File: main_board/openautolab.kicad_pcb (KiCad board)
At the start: 2 copper layers, 148.6 x 118.1 mm, 32 parts, among them J1 PIN11, J10 HX711, J11 LCD, J12 OUT+, J13 OUT-, J14 IN+, J15 IN-, J16 PWR_IN, J17 FILTER_PUMP, J18 FILTER_SENSOR, J2 PIN9, J3 PIN10, J4 PIN12, J6 PIN7, J7 PIN8, J8 PUMP, J9 SERVO, K1 FINDER-36.11, K2 FINDER-36.11, SW0 PIN_A0, SW1 PIN_A1, SW2 PIN_A2, SW3 SW_SPDT, U1 TD62064APG, U2 TD62064APG

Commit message: frame upgrades
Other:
- board size 148.6 x 118.1 mm -> 157.5 x 124.5 mm
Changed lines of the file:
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@@
     )
     (pad_to_mask_clearance 0)
+    (aux_axis_origin 27.94 22.86)
+    (grid_origin 27.94 22.86)
     (pcbplotparams
       (layerselection 0x00010fc_ffffffff)
@@
     )
   )
-  (gr_rect (start 32.38 27.3) (end 180.97 145.41) (layer "Edge.Cuts") (width 0.1) (fill none))
+  (gr_rect (start 39.37 93.98) (end 114.3 125.73) (layer "Dwgs.User") (width 0.15) (fill none))
+  (gr_rect (start 27.94 22.86) (end 185.42 147.32) (layer "Edge.Cuts") (width 0.1) (fill none))
   (segment (start 117.475 95.875) (end 120.01 95.875) (width 0.5) (layer "B.Cu") (net 4))
   (segment (start 36.195 142.87) (end 36.2 142.865) (width 0.5) (layer "B.Cu") (net 4))
@@
     (connect_pads (clearance 2))
     (min_thickness 1) (filled_areas_thickness no)
-    (fill yes (thermal_gap 0.508) (thermal_bridge_width 1) (island_removal_mode 2) (island_area_min 25))
+    (fill (thermal_gap 0.508) (thermal_bridge_width 1) (island_removal_mode 2) (island_area_min 25))
     (polygon
       (pts
-        (xy 180.97 145.41)
-        (xy 32.38 145.41)
-        (xy 32.38 27.3)
-        (xy 180.97 27.3)
+        (xy 185.42 147.32)
+        (xy 27.94 147.32)
+        (xy 27.94 22.86)
+        (xy 185.42 22.86)
       )
     )

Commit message: update PCB
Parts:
- removed J12: OUT+, Connector_PinHeader_2.54mm:PinHeader_1x01_P2.54mm_Vertical
- removed J13: OUT-, Connector_PinHeader_2.54mm:PinHeader_1x01_P2.54mm_Vertical
- removed J14: IN+, Connector_PinHeader_2.54mm:PinHeader_1x01_P2.54mm_Vertical
- removed J15: IN-, Connector_PinHeader_2.54mm:PinHeader_1x01_P2.54mm_Vertical
- added C1: C_Polarized, Capacitor_THT:CP_Radial_D10.0mm_P5.00mm, F.Cu at (147.3, 86.4)
- added C2: C_Polarized, Capacitor_THT:CP_Radial_D8.0mm_P5.00mm, F.Cu at (154.9, 59.8)
- added D6: 1N5822, Diode_THT:D_DO-201AD_P15.24mm_Horizontal, F.Cu at (145.4, 71.1)
- added L1: L, Inductor_THT:L_Toroid_Vertical_L26.7mm_W14.0mm_P10.16mm_Pulse_D, F.Cu at (172.7, 66.6)
- added NT1: NetTie_2, NetTie:NetTie-2_SMD_Pad2.0mm, F.Cu at (160.7, 50.8)
- added U3: LM2576T-5, Package_TO_SOT_THT:TO-220-5_Vertical, F.Cu at (151.7, 68.9)
- J16: value PWR_IN -> - PWR_IN +
- SW3: value SW_SPDT -> SW_DPST_x2; footprint Button_Switch_THT:SW_Slide_1P2T_CK_OS102011MS2Q -> Connector_PinHeader_2.54mm:PinHeader_1x02_P2.54mm_Vertical
- moved SW3 133.7 mm to (40.6, 58.4), turned to 180 degrees
- moved J17 89.8 mm to (148.6, 44.8), turned to 0 degrees
- moved D5 89.5 mm to (142.5, 54.5), turned to -90 degrees
- moved J18 80.1 mm to (135.9, 44.8), turned to 0 degrees
- moved A1 74.5 mm to (135.9, 111.8), turned to 90 degrees
- moved K2 62.4 mm to (104.1, 71.1)
- moved J9 60.4 mm to (40.6, 71.1), turned to 180 degrees
- moved K1 60.1 mm to (83.8, 71.1)
- moved J2 49.2 mm to (47.0, 44.8)
- moved J10 48.5 mm to (72.2, 92.7)
- moved J11 46.6 mm to (91.4, 92.7)
- moved BZ0 45.3 mm to (133.4, 83.8), turned to 0 degrees
- moved U1 42.8 mm to (69.7, 72.3), turned to 180 degrees
- moved SW2 33.8 mm to (131.8, 116.9)
- moved SW0 33.8 mm to (70.9, 117.2)
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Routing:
- net +12V: track 595.9 -> 250.1 mm, vias 0 -> 1
- net GNDPWR: track 382.9 -> 184.2 mm, vias 4 -> 1
- net Net-(A1-Pad5): track 224.5 -> 89.8 mm
- net Net-(A1-Pad6): track 225.7 -> 91.2 mm
- net Net-(D5-Pad2): track 18.5 -> 139.2 mm, vias 0 -> 1
- net Net-(A1-Pad14): track 17.5 -> 133.4 mm, vias 0 -> 2
- net GND: track 417.6 -> 305.7 mm, vias 4 -> 1
- net Net-(A1-Pad15): track 42.9 -> 145.2 mm, vias 2 -> 1
- net Net-(A1-Pad13): track 56.3 -> 150.9 mm, vias 2 -> 0
- net Net-(A1-Pad7): track 46.5 -> 135.7 mm
- net Net-(J18-Pad2): track 19.9 -> 107.6 mm
- net Net-(A1-Pad12): track 46.8 -> 133.7 mm, vias 0 -> 1
- net Net-(A1-Pad21): track 123.3 -> 37.3 mm
- net +5V: track 226.7 -> 157.1 mm, vias 0 -> 2
- net Net-(J4-Pad1): track 13.9 -> 61.9 mm
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- removed copper zone on B.Cu, net GNDPWR
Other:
- board size 157.5 x 124.5 mm -> 144.8 x 88.9 mm

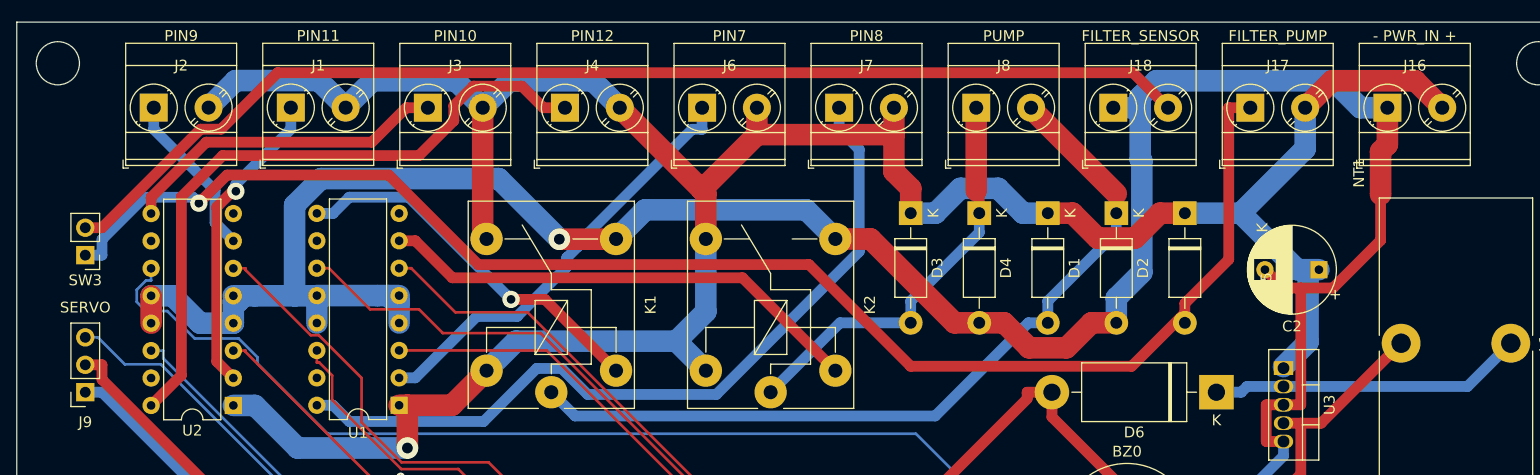
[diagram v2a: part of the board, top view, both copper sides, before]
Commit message: update schematic add power switch
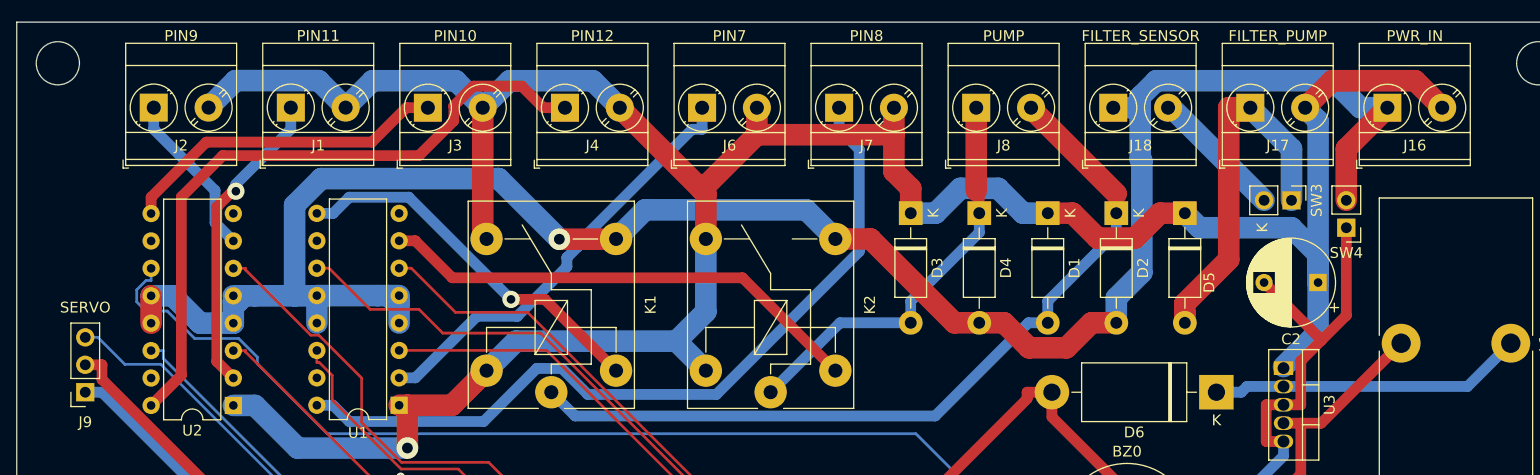
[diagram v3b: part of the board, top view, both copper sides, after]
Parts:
- removed NT1: NetTie_2, NetTie:NetTie-2_SMD_Pad2.0mm
- added SW4: SW_DPST_x2, Connector_PinHeader_2.54mm:PinHeader_1x02_P2.54mm_Vertical, F.Cu at (157.5, 55.9)
- J16: value - PWR_IN + -> PWR_IN
- moved SW3 111.9 mm to (152.4, 53.3), turned to -90 degrees
- moved C2 1.20 mm to (154.9, 61.0)
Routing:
- net Net-(D5-A): track 139.2 -> 33.8 mm, vias 1 -> 0
- net Net-(J18-Pin_2): track 107.6 -> 12.4 mm
- net GNDPWR: track 184.2 -> 190.0 mm
- net +12V: track 250.1 -> 255.7 mm
- net GND: track 305.7 -> 303.0 mm

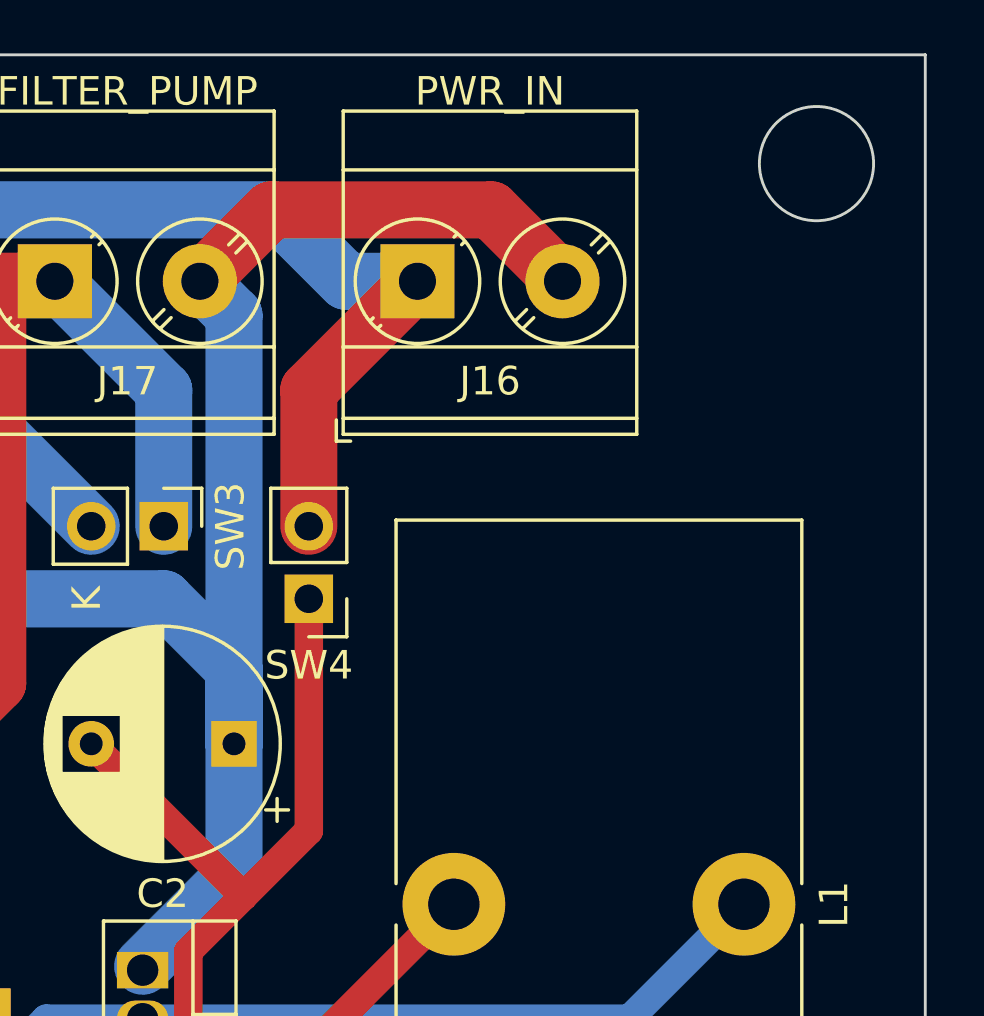
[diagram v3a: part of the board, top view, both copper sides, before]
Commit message: fixed power switch on board
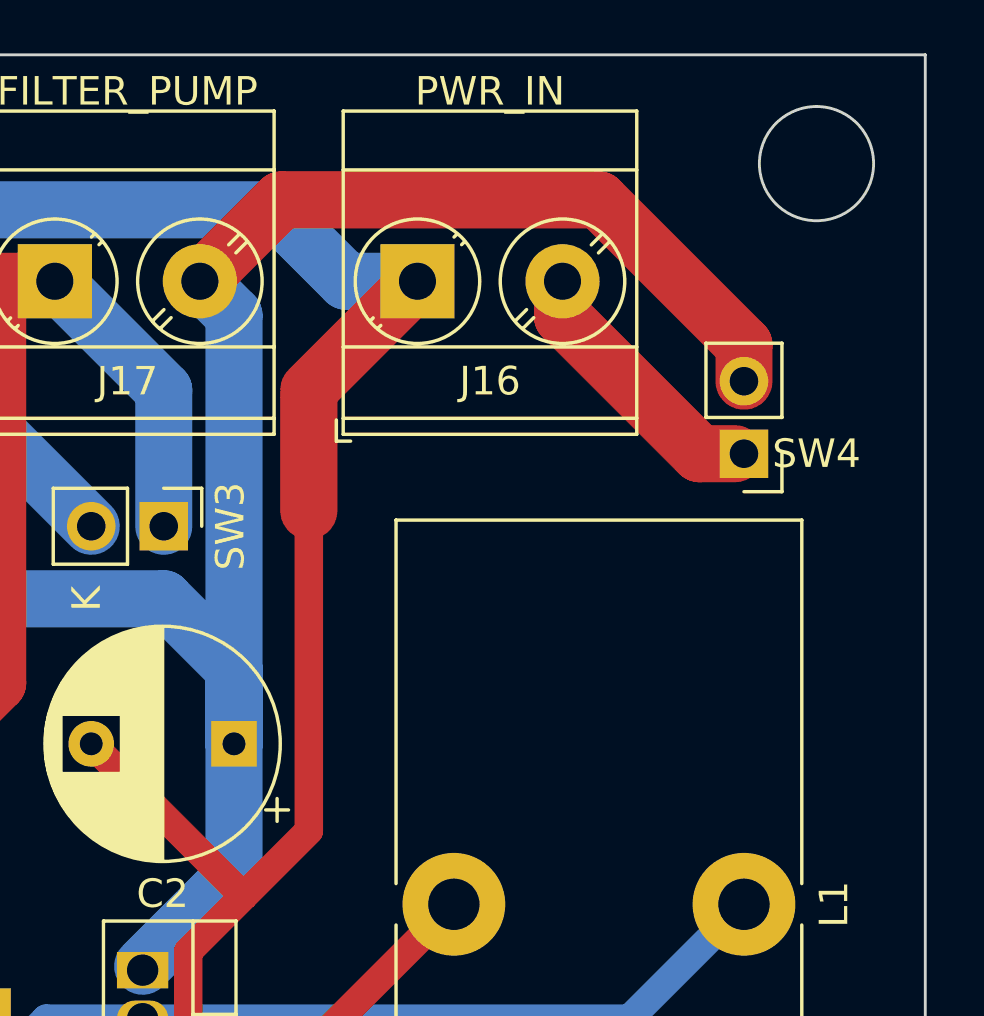
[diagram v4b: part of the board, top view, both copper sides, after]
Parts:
- added NT1: NetTie_2, NetTie:NetTie-2_SMD_Pad2.0mm, F.Cu at (157.5, 50.8)
- moved SW4 16.1 mm to (172.7, 50.8)
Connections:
- J16 pad 2: +12V -> Net-(J16-Pin_2)
- SW4 pad 1: GND -> Net-(J16-Pin_2)
- SW4 pad 2: GNDPWR -> +12V
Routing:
- net Net-(J16-Pin_2): track 0.00 -> 9.58 mm
- net +12V: track 255.7 -> 264.5 mm
- net GNDPWR: track 190.0 -> 185.2 mm
- net GND: track 303.0 -> 306.1 mm
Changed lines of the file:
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@@
   (net 43 "Net-(U1-O2)")
   (net 44 "GNDPWR")
+  (net 45 "Net-(J16-Pin_2)")
   (footprint "TerminalBlock_Phoenix:TerminalBlock_Phoenix_MKDS-3-2-5.08_1x02_P5.08mm_Horizontal" (layer "F.Cu")
     (at 161.285 44.76)
@@
       (net 44 "GNDPWR") (pinfunction "Pin_1") (pintype "passive"))
     (pad "2" thru_hole circle (at 5.08 0) (size 2.6 2.6) (drill 1.3) (layers "F&B.Cu" "*.Mask")
-      (net 42 "+12V") (pinfunction "Pin_2") (pintype "passive"))
+      (net 45 "Net-(J16-Pin_2)") (pinfunction "Pin_2") (pintype "passive"))
     (model "${KICAD6_3DMODEL_DIR}/TerminalBlock_Phoenix.3dshapes/TerminalBlock_Phoenix_MKDS-3-2-5.08_1x02_P5.08mm_Horizontal.wrl"
       (offset (xyz 0 0 0))
@@
   )
   (footprint "Connector_PinHeader_2.54mm:PinHeader_1x02_P2.54mm_Vertical" (layer "F.Cu")
-    (at 157.48 55.88 180)
+    (at 172.72 50.8 180)
     (descr "Through hole straight pin header, 1x02, 2.54mm pitch, single row")
     (tags "Through hole pin header THT 1x02 2.54mm single row")
@@
     (property "ki_keywords" "switch lever")
     (attr through_hole)
-    (fp_text reference "SW4" (at 0 -2.33) (layer "F.SilkS")
+    (fp_text reference "SW4" (at -2.54 0) (layer "F.SilkS")
         (effects (font (size 1 1) (thickness 0.15)))
     )
@@
       (stroke (width 0.1) (type solid)) (layer "F.Fab"))
     (pad "1" thru_hole rect (at 0 0 180) (size 1.7 1.7) (drill 1) (layers "*.Cu" "*.Mask")
-      (net 30 "GND") (pinfunction "A") (pintype "passive"))
+      (net 45 "Net-(J16-Pin_2)") (pinfunction "A") (pintype "passive"))
     (pad "2" thru_hole oval (at 0 2.54 180) (size 1.7 1.7) (drill 1) (layers "*.Cu" "*.Mask")
-      (net 44 "GNDPWR") (pinfunction "B") (pintype "passive"))
+      (net 42 "+12V") (pinfunction "B") (pintype "passive"))
     (model "${KICAD6_3DMODEL_DIR}/Connector_PinHeader_2.54mm.3dshapes/PinHeader_1x02_P2.54mm_Vertical.wrl"
       (offset (xyz 0 0 0))
@@
     )
   )
+  (footprint "NetTie:NetTie-2_SMD_Pad2.0mm" (layer "F.Cu")
+    (at 157.48 50.8 90)
+    (descr "Net tie, 2 pin, 2.0mm square SMD pads")
+    (tags "net tie")
+    (property "Sheetfile" "openautolab.kicad_sch")
+    (property "Sheetname" "")
+    (property "exclude_from_bom" "")
+    (property "ki_description" "Net tie, 2 pins")
+    (property "ki_keywords" "net tie short")
+    (attr exclude_from_pos_files exclude_from_bom allow_missing_courtyard)
+    (net_tie_pad_groups "1, 2")
+    (fp_text reference "NT1" (at 0 -2 90) (layer "F.SilkS") hide
+        (effects (font (size 1 1) (thickness 0.15)))
+    )
+    (fp_text value "NetTie_2" (at 0 2 90) (layer "F.Fab") hide
+        (effects (font (size 1 1) (thickness 0.15)))
+    )
+    (fp_poly
+      (pts
+        (xy -2 -1)
+        (xy 2 -1)
+        (xy 2 1)
+        (xy -2 1)
+      )
+      (stroke (width 0) (type solid)) (fill solid) (layer "F.Cu"))
+    (pad "1" smd circle (at -2 0 90) (size 2 2) (layers "F.Cu")
+      (net 30 "GND") (pinfunction "1") (pintype "passive"))
+    (pad "2" smd circle (at 2 0 90) (size 2 2) (layers "F.Cu")
+      (net 44 "GNDPWR") (pinfunction "2") (pintype "passive"))
+  )
   (footprint "Capacitor_THT:CP_Radial_D10.0mm_P5.00mm" (layer "F.Cu")
     (at 147.32 86.36)
@@
   (segment (start 72.6006 94.6157) (end 72.25 94.2651) (width 1) (layer "F.Cu") (net 30))
   (segment (start 72.6006 121.6656) (end 70.87 121.6656) (width 1) (layer "F.Cu") (net 30))
+  (segment (start 155.1938 66.2938) (end 157.48 64.0076) (width 1) (layer "F.Cu") (net 30))
   (segment (start 140.515 83.82) (end 140.515 83.7301) (width 1) (layer "F.Cu") (net 30))
   (segment (start 138.43 96.51) (end 138.43 95.0099) (width 1) (layer "F.Cu") (net 30))
@@
   (segment (start 151.4628 72.287) (end 151.66 72.287) (width 1) (layer "F.Cu") (net 30))
   (segment (start 151.66 75.687) (end 150.0599 75.687) (width 1) (layer "F.Cu") (net 30))
-  (segment (start 157.48 64.0076) (end 157.48 55.88) (width 1) (layer "F.Cu") (net 30))
   (segment (start 89.8649 92.7) (end 89.8499 92.715) (width 1) (layer "F.Cu") (net 30))
   (segment (start 72.25 92.715) (end 72.25 94.2651) (width 1) (layer "F.Cu") (net 30))
@@
   (segment (start 91.415 92.7) (end 89.8649 92.7) (width 1) (layer "F.Cu") (net 30))
   (segment (start 130.205 71.12) (end 127.9049 71.12) (width 1) (layer "F.Cu") (net 30))
-  (segment (start 155.1938 66.2938) (end 157.48 64.0076) (width 1) (layer "F.Cu") (net 30))
   (segment (start 110.182 89.4565) (end 127.9049 71.7336) (width 1) (layer "F.Cu") (net 30))
   (segment (start 149.86 60.96) (end 155.1938 66.2938) (width 1) (layer "F.Cu") (net 30))
@@
   (segment (start 150.0599 72.287) (end 150.0599 75.687) (width 1) (layer "F.Cu") (net 30))
   (segment (start 130.205 71.12) (end 130.205 73.4201) (width 1) (layer "F.Cu") (net 30))
+  (segment (start 157.48 64.0076) (end 157.48 52.8) (width 1) (layer "F.Cu") (net 30))
   (segment (start 89.8499 92.715) (end 72.25 92.715) (width 1) (layer "F.Cu") (net 30))
   (segment (start 131.83 121.3706) (end 108.145 121.3706) (width 1) (layer "F.Cu") (net 30))
@@
   (segment (start 63.6001 54.55) (end 65.1004 53.0497) (width 1) (layer "B.Cu") (net 41))
   (segment (start 62.1 54.55) (end 63.6001 54.55) (width 1) (layer "B.Cu") (net 41))
+  (segment (start 156.515 41.91) (end 167.64 41.91) (width 2) (layer "F.Cu") (net 42))
+  (segment (start 153.665 44.76) (end 156.515 41.91) (width 2) (layer "F.Cu") (net 42))
   (segment (start 129.82 54.53) (end 132.1201 54.53) (width 2) (layer "F.Cu") (net 42))
   (segment (start 132.1201 54.53) (end 134.4202 56.8301) (width 2) (layer "F.Cu") (net 42))
@@
   (segment (start 77.465 56.565) (end 77.82 56.92) (width 2) (layer "F.Cu") (net 42))
   (segment (start 98.14 56.92) (end 98.14 52.735) (width 2) (layer "F.Cu") (net 42))
+  (segment (start 167.64 41.91) (end 172.72 46.99) (width 2) (layer "F.Cu") (net 42))
   (segment (start 70.4875 72.33) (end 69.72 72.33) (width 2) (layer "F.Cu") (net 42))
   (segment (start 115.565 47.2602) (end 115.565 44.76) (width 2) (layer "F.Cu") (net 42))
@@
   (segment (start 98.14 52.735) (end 97.7676 52.3626) (width 2) (layer "F.Cu") (net 42))
   (segment (start 117.12 52.2299) (end 115.565 50.6749) (width 2) (layer "F.Cu") (net 42))
-  (segment (start 153.665 44.76) (end 156.1652 42.2598) (width 2) (layer "F.Cu") (net 42))
-  (segment (start 156.1652 42.2598) (end 163.8648 42.2598) (width 2) (layer "F.Cu") (net 42))
   (segment (start 102.87 47.2602) (end 102.87 44.76) (width 2) (layer "F.Cu") (net 42))
   (segment (start 134.4202 56.8301) (end 137.9198 56.8301) (width 2) (layer "F.Cu") (net 42))
   (segment (start 117.12 54.53) (end 117.12 52.2299) (width 2) (layer "F.Cu") (net 42))
   (segment (start 77.465 44.76) (end 77.465 56.565) (width 2) (layer "F.Cu") (net 42))
-  (segment (start 163.8648 42.2598) (end 166.365 44.76) (width 2) (layer "F.Cu") (net 42))
+  (segment (start 172.72 46.99) (end 172.72 48.26) (width 2) (layer "F.Cu") (net 42))
   (segment (start 102.87 47.2602) (end 115.565 47.2602) (width 2) (layer "F.Cu") (net 42))
   (segment (start 115.565 50.6749) (end 115.565 47.2602) (width 2) (layer "F.Cu") (net 42))
@@
   (segment (start 157.48 48.565) (end 161.285 44.76) (width 2) (layer "F.Cu") (net 44))
   (segment (start 89.7965 56.9435) (end 89.82 56.92) (width 2) (layer "F.Cu") (net 44))
-  (segment (start 157.48 53.34) (end 157.48 48.565) (width 2) (layer "F.Cu") (net 44))
   (via (at 84.563 56.9435) (size 2) (drill 1) (layers "F.Cu" "B.Cu") (net 44))
   (segment (start 68.72 62.17) (end 69.2599 62.7099) (width 2) (layer "B.Cu") (net 44))
@@
   (segment (start 92.5208 54.2192) (end 107.4392 54.2192) (width 2) (layer "B.Cu") (net 44))
   (segment (start 54.36 62.185) (end 55.3601 62.185) (width 2) (layer "B.Cu") (net 44))
+  (segment (start 171.164365 50.8) (end 172.405 50.8) (width 2) (layer "F.Cu") (net 45))
+  (segment (start 166.365 44.76) (end 166.365 46.000635) (width 2) (layer "F.Cu") (net 45))
+  (segment (start 166.365 46.000635) (end 171.164365 50.8) (width 2) (layer "F.Cu") (net 45))
+  (segment (start 172.405 50.8) (end 172.72 50.8) (width 0.25) (layer "F.Cu") (net 45))
 )
